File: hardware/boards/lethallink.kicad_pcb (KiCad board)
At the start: 6 copper layers, 86 x 111.1 mm, 138 parts, among them J1 PCIe-x4, J2 USB3_Micro_B_Amphenol, Q1 Q_NMOS_GSD, Q2 Q_NMOS_GSD, Q3 Q_NMOS_GSD, Q4 Q_NMOS_GSD, Q5 SI7232DN-T1-GE3, SW1 SW_DIP_x03, U1 ECP5UM5G-381caBGA, U2 ADP5050ACPZ-R7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

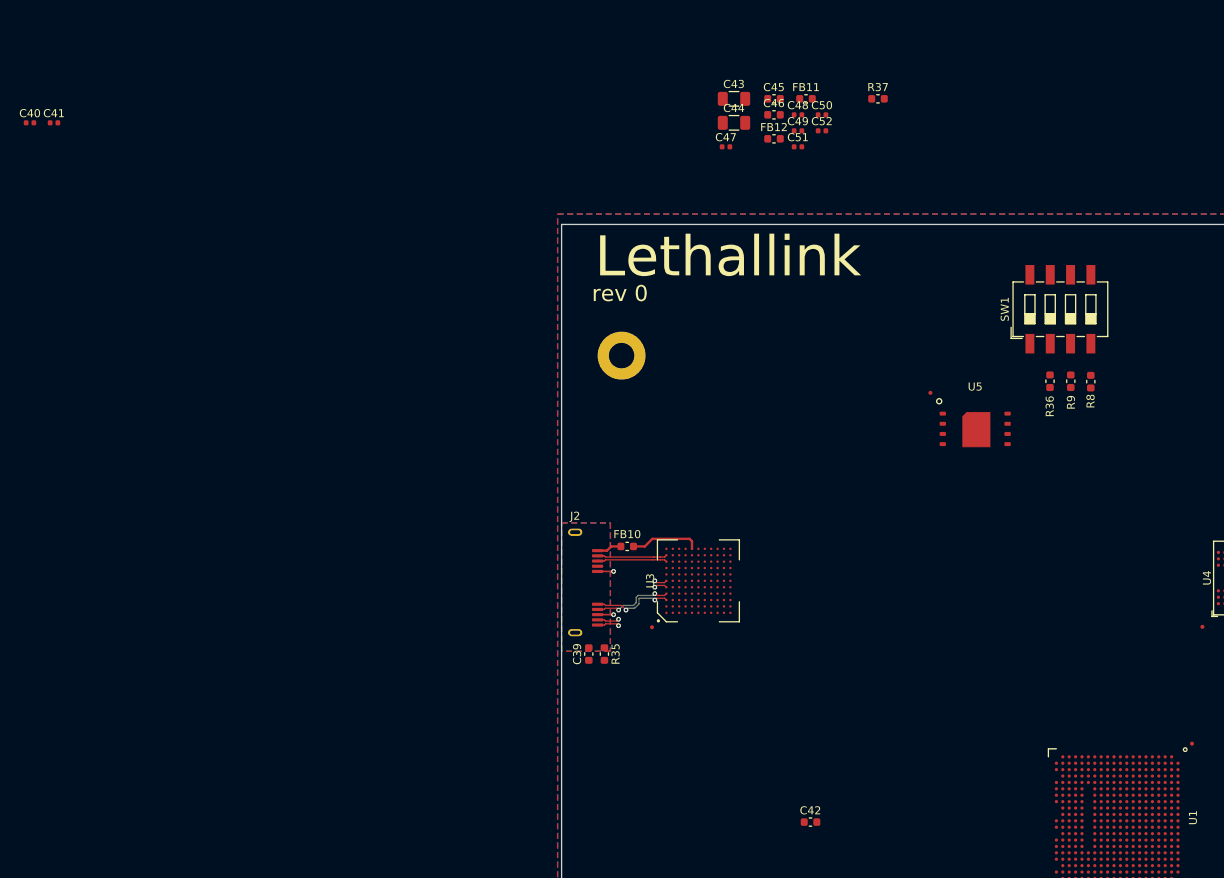
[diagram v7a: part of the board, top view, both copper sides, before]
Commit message: Added the JTAG header and some misc cleanup
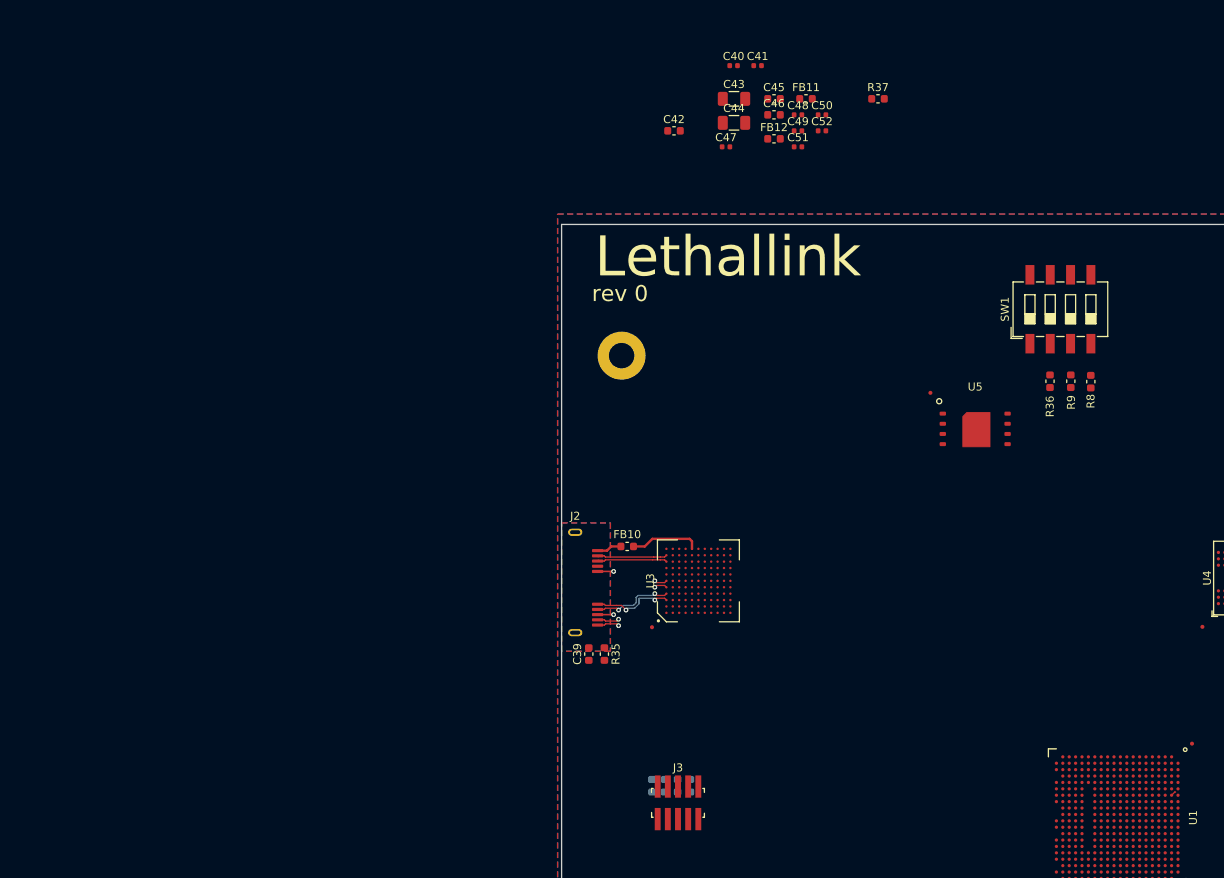
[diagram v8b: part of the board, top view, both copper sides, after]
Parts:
- added J3: Conn_02x05_Odd_Even, lethalbit-connectors:FTSH-105-01-L-DV-K-TR, F.Cu at (32.0, 88.0)
- added R38: 10k, Resistor_SMD:R_0603_1608Metric, B.Cu at (28.8, 85.9)
- added R39: 10k, Resistor_SMD:R_0603_1608Metric, B.Cu at (30.4, 85.9)
- added R40: 10k, Resistor_SMD:R_0603_1608Metric, B.Cu at (31.9, 85.9)
- added R41: 10k, Resistor_SMD:R_0603_1608Metric, B.Cu at (33.5, 85.9)
- moved C40 88.2 mm to (39.0, -4.15)
- moved C41 88.2 mm to (42.0, -4.15)
- moved C42 88.1 mm to (31.5, 4.00)
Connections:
- U1 pad T5: Net-(U1-PadT5) -> Net-(J3-Pad4)
- U1 pad U5: Net-(U1-PadU5) -> Net-(J3-Pad2)
- U3 pad E7: Net-(U3-PadE7) -> Net-(U1-PadV4)
- U3 pad E8: Net-(U3-PadE8) -> Net-(J3-Pad2)
- U3 pad F6: Net-(U3-PadF6) -> Net-(J3-Pad4)
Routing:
- net GND: track 59.5 -> 60.2 mm
